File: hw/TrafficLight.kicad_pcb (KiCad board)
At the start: 2 copper layers, 95 x 55 mm, 14 parts, among them IC1 ATTINY85-P, P1 HC-SR04 Header, P2 LED and Power Header, Q1 PN2222A, Q2 PN2222A, Q3 PN2222A

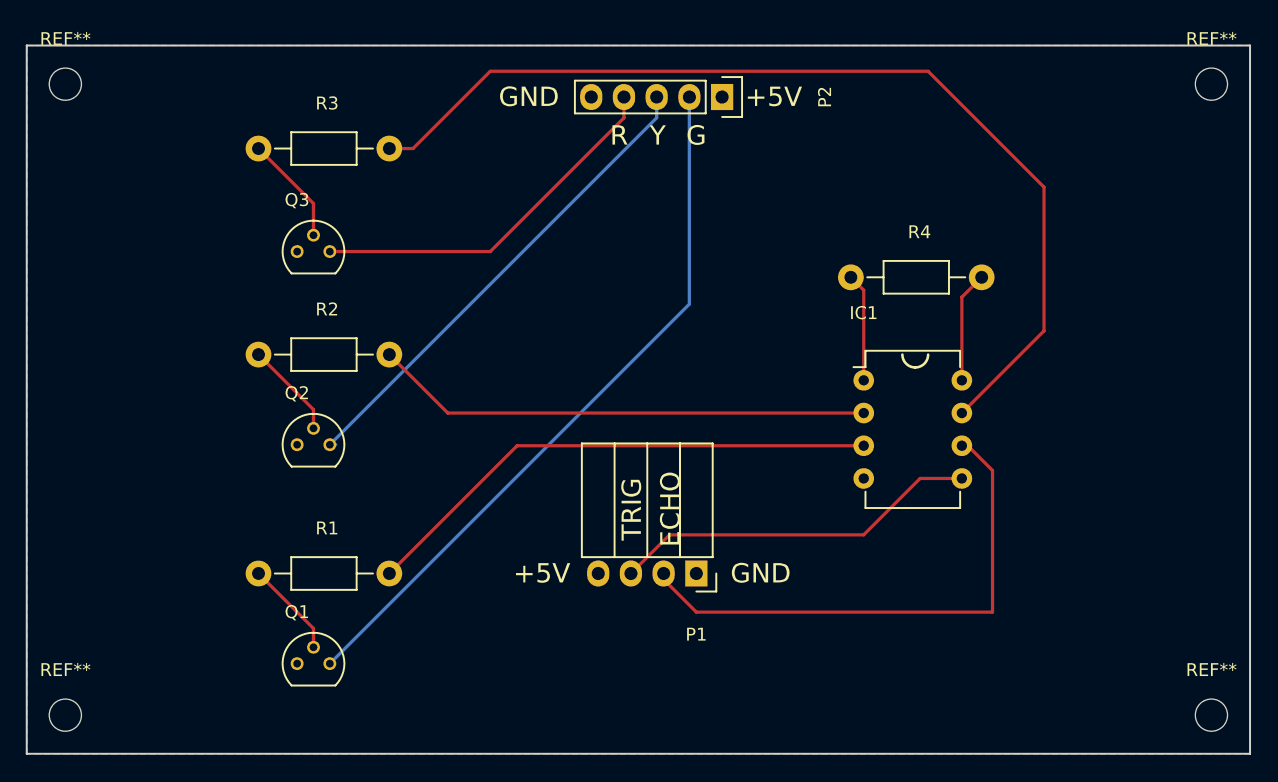
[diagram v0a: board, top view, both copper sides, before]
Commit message: Fix up PCB layout, fix directory names
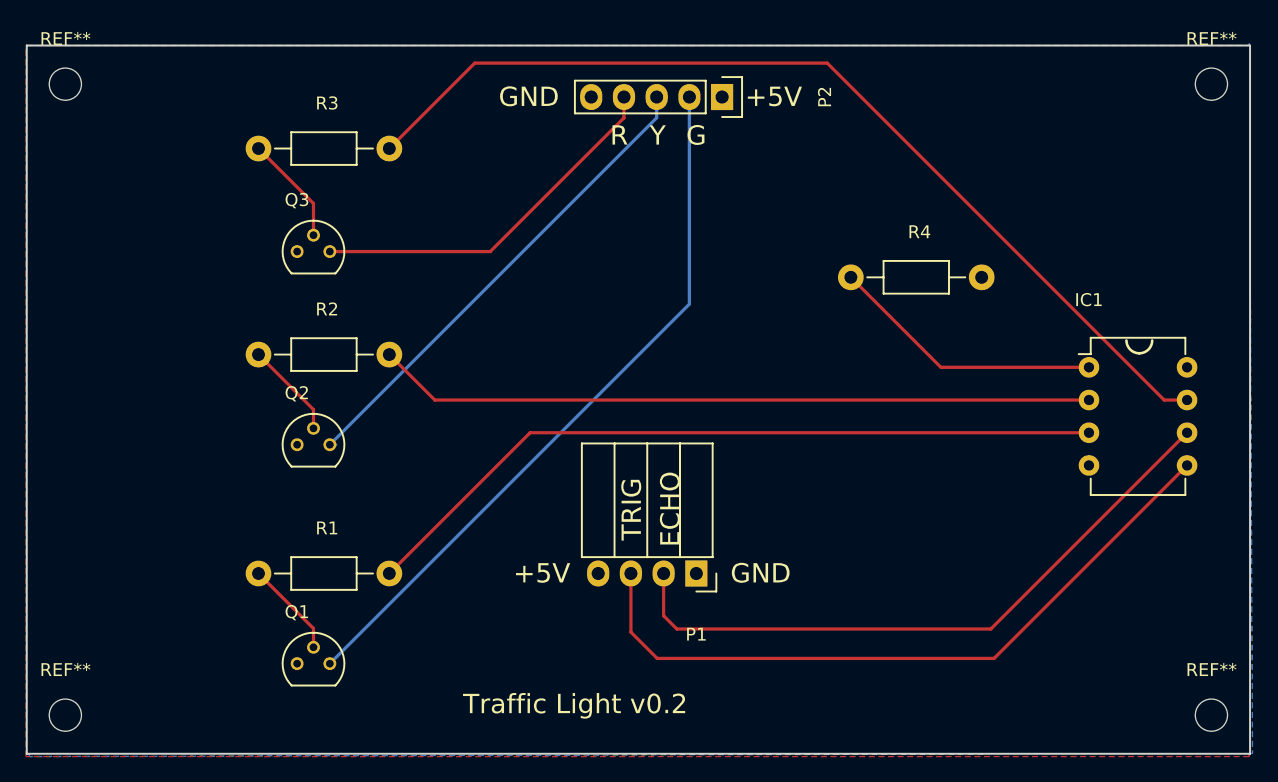
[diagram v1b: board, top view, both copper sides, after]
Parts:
- moved IC1 17.5 mm to (110.5, 47.0)
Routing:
- net /TRIG: track 28.8 -> 54.8 mm
- net /GREEN: track 41.1 -> 59.0 mm
- net /YELLOW: track 38.7 -> 55.8 mm
- net Net-(IC1-Pad1): track 8.41 -> 21.4 mm
- net /ECHO: track 41.5 -> 51.1 mm
- net +5V: track 8.64 -> 0.00 mm
- net /RED: track 77.2 -> 75.5 mm
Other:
- board text added: "Traffic Light v0.2"
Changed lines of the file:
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@@
-(kicad_pcb (version 4) (host pcbnew 4.0.5+dfsg1-4)
+(kicad_pcb (version 4) (host pcbnew 4.0.7)
   (general
     (links 20)
     (no_connects 0)
-    (area 22.871429 17.133332 128.128572 78.575)
+    (area 27.924999 21.924999 123.075001 77.075001)
     (thickness 1.6)
-    (drawings 15)
-    (tracks 40)
+    (drawings 16)
+    (tracks 34)
     (zones 0)
     (modules 14)
@@
     (pad_to_mask_clearance 0.2)
     (aux_axis_origin 0 0)
-    (visible_elements FFFFFF7F)
+    (visible_elements 7FFFFFFF)
     (pcbplotparams
       (layerselection 0x010f0_80000001)
@@
   )
   (module Housings_DIP:DIP-8_W7.62mm (layer F.Cu)
-    (at 93 48)
+    (at 110.49 46.99)
     (descr "8-lead dip package, row spacing 7.62 mm (300 mils)")
     (tags "dil dip 2.54 300")
@@
     )
   )
-  (gr_arc (start 97 46) (end 98 46) (angle 90) (layer F.SilkS) (width 0.2))
-  (gr_arc (start 97 46) (end 97 47) (angle 90) (layer F.SilkS) (width 0.2))
+  (gr_text "Traffic Light v0.2" (at 70.612 73.152) (layer F.SilkS)
+    (effects (font (size 1.5 1.5) (thickness 0.3)))
+  )
+  (gr_arc (start 114.4 44.9) (end 115.4 44.9) (angle 90) (layer F.SilkS) (width 0.2))
+  (gr_arc (start 114.4 44.9) (end 114.4 45.9) (angle 90) (layer F.SilkS) (width 0.2))
   (gr_text ECHO (at 78 58 90) (layer F.SilkS)
     (effects (font (size 1.5 1.5) (thickness 0.3)))
@@
   (gr_line (start 123 22) (end 123 77) (angle 90) (layer Edge.Cuts) (width 0.15))
   (gr_line (start 28 22) (end 123 22) (angle 90) (layer Edge.Cuts) (width 0.15))
-  (segment (start 93 48) (end 93 41) (width 0.25) (layer F.Cu) (net 1))
-  (segment (start 93 41) (end 92 40) (width 0.25) (layer F.Cu) (net 1))
-  (segment (start 93 50.54) (end 60.7 50.54) (width 0.25) (layer F.Cu) (net 2))
-  (segment (start 60.7 50.54) (end 56.16 46) (width 0.25) (layer F.Cu) (net 2))
-  (segment (start 93 53.08) (end 66.08 53.08) (width 0.25) (layer F.Cu) (net 3))
-  (segment (start 66.08 53.08) (end 56.16 63) (width 0.25) (layer F.Cu) (net 3))
+  (segment (start 110.49 46.99) (end 98.99 46.99) (width 0.25) (layer F.Cu) (net 1))
+  (segment (start 98.99 46.99) (end 92 40) (width 0.25) (layer F.Cu) (net 1))
+  (segment (start 110.49 49.53) (end 59.69 49.53) (width 0.25) (layer F.Cu) (net 2))
+  (segment (start 59.69 49.53) (end 56.16 46) (width 0.25) (layer F.Cu) (net 2))
+  (segment (start 110.49 52.07) (end 67.09 52.07) (width 0.25) (layer F.Cu) (net 3))
+  (segment (start 67.09 52.07) (end 56.16 63) (width 0.25) (layer F.Cu) (net 3))
   (segment (start 56.16 63) (end 56.16 62.84) (width 0.25) (layer B.Cu) (net 3))
-  (segment (start 100.62 55.62) (end 97.38 55.62) (width 0.25) (layer F.Cu) (net 5))
-  (segment (start 77.92 60) (end 74.92 63) (width 0.25) (layer F.Cu) (net 5))
-  (segment (start 93 60) (end 77.92 60) (width 0.25) (layer F.Cu) (net 5))
-  (segment (start 97.38 55.62) (end 93 60) (width 0.25) (layer F.Cu) (net 5))
-  (segment (start 100.62 53.08) (end 101.08 53.08) (width 0.25) (layer F.Cu) (net 6))
-  (segment (start 101.08 53.08) (end 103 55) (width 0.25) (layer F.Cu) (net 6))
-  (segment (start 80 66) (end 77.46 63.46) (width 0.25) (layer F.Cu) (net 6))
-  (segment (start 103 66) (end 80 66) (width 0.25) (layer F.Cu) (net 6))
-  (segment (start 103 55) (end 103 66) (width 0.25) (layer F.Cu) (net 6))
+  (segment (start 74.92 63) (end 74.92 67.554) (width 0.25) (layer F.Cu) (net 5))
+  (segment (start 103.124 69.596) (end 118.11 54.61) (width 0.25) (layer F.Cu) (net 5))
+  (segment (start 76.962 69.596) (end 103.124 69.596) (width 0.25) (layer F.Cu) (net 5))
+  (segment (start 74.92 67.554) (end 76.962 69.596) (width 0.25) (layer F.Cu) (net 5))
+  (segment (start 77.46 63) (end 77.46 66.284) (width 0.25) (layer F.Cu) (net 6))
+  (segment (start 102.87 67.31) (end 118.11 52.07) (width 0.25) (layer F.Cu) (net 6))
+  (segment (start 78.486 67.31) (end 102.87 67.31) (width 0.25) (layer F.Cu) (net 6))
+  (segment (start 77.46 66.284) (end 78.486 67.31) (width 0.25) (layer F.Cu) (net 6))
   (segment (start 77.46 63.46) (end 77.46 63) (width 0.25) (layer F.Cu) (net 6))
-  (segment (start 100.62 53.08) (end 100.62 53.38) (width 0.25) (layer F.Cu) (net 6))
-  (segment (start 56.16 30) (end 58 30) (width 0.25) (layer F.Cu) (net 7))
-  (segment (start 107 44.16) (end 100.62 50.54) (width 0.25) (layer F.Cu) (net 7))
-  (segment (start 107 33) (end 107 44.16) (width 0.25) (layer F.Cu) (net 7))
-  (segment (start 98 24) (end 107 33) (width 0.25) (layer F.Cu) (net 7))
-  (segment (start 64 24) (end 98 24) (width 0.25) (layer F.Cu) (net 7))
-  (segment (start 58 30) (end 64 24) (width 0.25) (layer F.Cu) (net 7))
-  (segment (start 100.62 48) (end 100.62 41.54) (width 0.25) (layer F.Cu) (net 8))
-  (segment (start 100.62 41.54) (end 102.16 40) (width 0.25) (layer F.Cu) (net 8))
+  (segment (start 118.11 49.53) (end 116.332 49.53) (width 0.25) (layer F.Cu) (net 7))
+  (segment (start 62.792 23.368) (end 56.16 30) (width 0.25) (layer F.Cu) (net 7))
+  (segment (start 90.17 23.368) (end 62.792 23.368) (width 0.25) (layer F.Cu) (net 7))
+  (segment (start 116.332 49.53) (end 90.17 23.368) (width 0.25) (layer F.Cu) (net 7))
   (segment (start 50.27 68.73) (end 50.27 67.27) (width 0.25) (layer F.Cu) (net 9))
   (segment (start 50.27 67.27) (end 46 63) (width 0.25) (layer F.Cu) (net 9))
@@
     (polygon
       (pts
-        (xy 123 77) (xy 28 77) (xy 28 22) (xy 123 22)
+        (xy 122.936719 22) (xy 123 22) (xy 123 35.732) (xy 123.19 76.962) (xy 123 76.962508)
+        (xy 123 77) (xy 108.978 77) (xy 28.194 77.216) (xy 28.194 77) (xy 28 77)
+        (xy 28 22) (xy 122.936 22) (xy 122.936 21.844)
       )
     )
@@
     (polygon
       (pts
-        (xy 123 77) (xy 28 77) (xy 28 22) (xy 123 22)
+        (xy 123 77) (xy 122.936 77) (xy 122.936 77.216) (xy 27.94 77.216) (xy 27.94 22.098)
+        (xy 28 22.098) (xy 28 22) (xy 123 22)
       )
     )
